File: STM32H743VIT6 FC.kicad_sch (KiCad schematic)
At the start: 88 parts, among them SW2 SW_Push, U1 TPS54302DDCR, U2 USBLC6-2SC6, U3 TPS54302DDCR, U3_MUX1 TPS2121RUXR

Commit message: mux no no no
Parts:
- removed D_5V1, D_5V_USB1: B340A-13-F, custom_Library:Schottky BA340 SMA_L4.4-W2.6-LS5.0-RD, symbol custom_Library:B340A-13-F
- removed MUX_C2: 100n, Capacitor_SMD:C_0603_1608Metric, symbol Device:C_Small
- removed MUX_R10: 60, Resistor_SMD:R_0603_1608Metric, symbol Device:R_Small
- removed MUX_R6: 13k, Resistor_SMD:R_0603_1608Metric, symbol Device:R_Small
- removed MUX_R7, MUX_R9: 5k, Resistor_SMD:R_0603_1608Metric, symbol Device:R_Small
- removed MUX_R8: 43k, Resistor_SMD:R_0603_1608Metric, symbol Device:R_Small
- removed U3_MUX1: TPS2121RUXR, TPS2121RUXR:RUX0012A, symbol ul_TPS2121RUXR:TPS2121RUXR
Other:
- note removed: "Diodes: 40V/3A 500mV 850mW"
- note removed: "Power Mux"
- note removed: "Power Path"

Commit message: nez
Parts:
- 5V_R8: value 13k3 -> 13k
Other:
- note added: "BAT -> 5.2V @3A"
- note removed: "BAT -> 5V @3A"
- moved on the sheet: 3V3_C4, 3v3_C3, 5V_C10, 5V_C11, 5V_C12, 5V_C7, 5V_C8, 5V_C9, 5V_L2, 5V_R5, 5V_R6, 5V_R7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

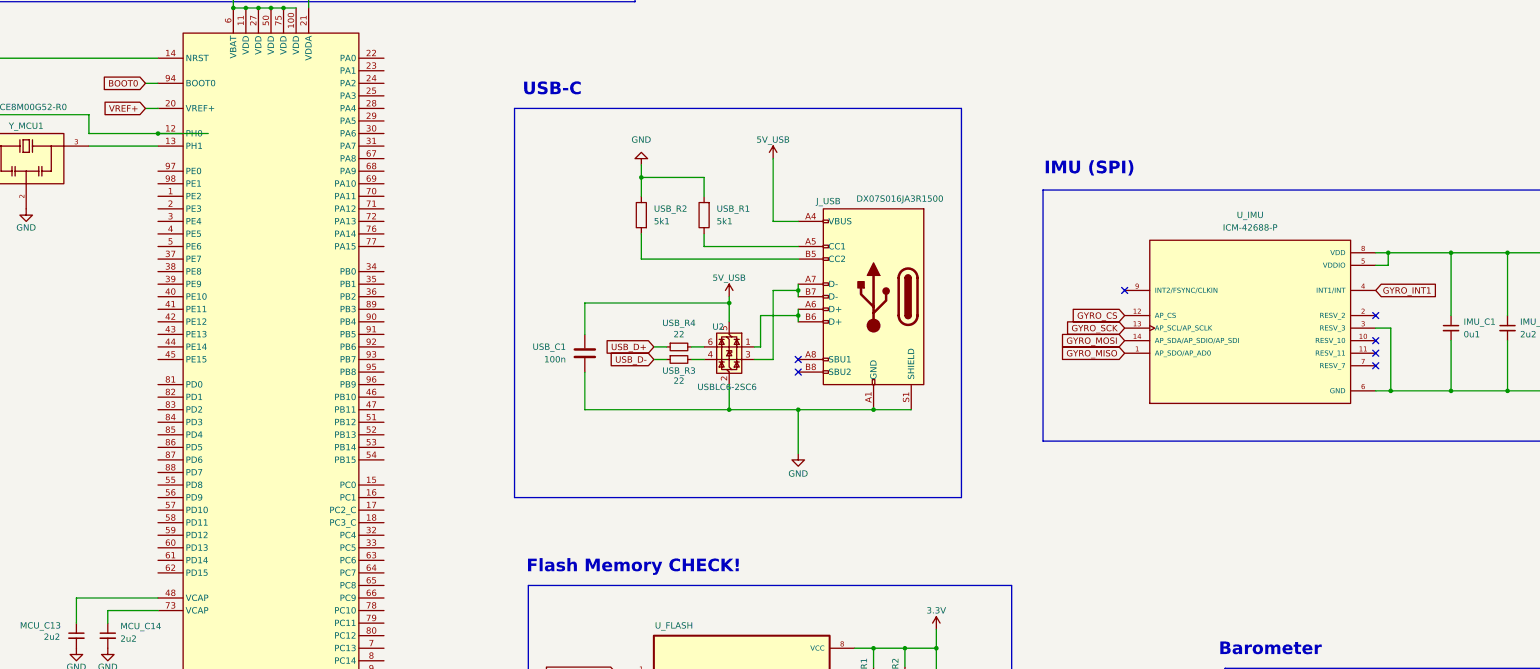
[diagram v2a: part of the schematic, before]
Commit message: Verified and connected IMU.
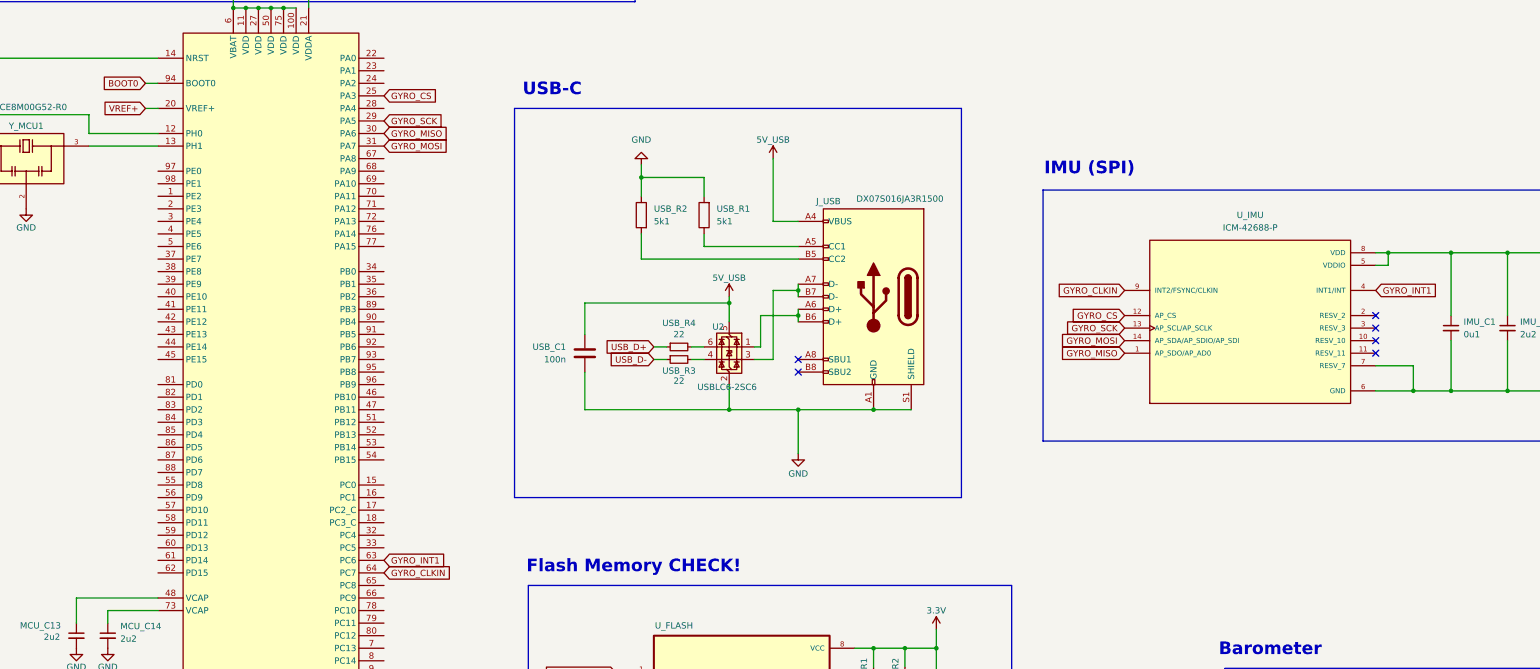
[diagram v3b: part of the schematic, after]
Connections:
- net GND: now also U_IMU.7 (RESV_7); no longer U_IMU.3 (RESV_3)
- net GYRO_CS: now also U_STM32.25 (PA3)
- net GYRO_INT1: now also U_STM32.63 (PC6)
- net GYRO_MISO: now also U_STM32.30 (PA6)
- net GYRO_MOSI: now also U_STM32.31 (PA7)
- net GYRO_SCK: now also U_STM32.29 (PA5)
- net GYRO_CLKIN: now reaches U_STM32.64 (PC7)
- net GYRO_CLKIN: now also U_IMU.9 (INT2/FSYNC/CLKIN)
- no-connect marks 9 -> 8
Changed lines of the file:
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@@
 	)
 	(junction
-		(at 102.87 93.98)
-		(diameter 0)
-		(color 0 0 0 0)
-	)
-	(junction
 		(at 487.68 323.85)
 		(diameter 0)
@@
 	)
 	(junction
-		(at 352.298 146.05)
-		(diameter 0)
-		(color 0 0 0 0)
-	)
-	(junction
 		(at 165.1 62.23)
 		(diameter 0)
@@
 	)
 	(junction
+		(at 356.87 146.05)
+		(diameter 0)
+		(color 0 0 0 0)
+	)
+	(junction
 		(at 88.9 54.61)
 		(diameter 0)
@@
 	)
 	(no_connect
+		(at 349.25 133.35)
+	)
+	(no_connect
 		(at 349.25 135.89)
 	)
@@
 	)
 	(no_connect
-		(at 298.45 125.73)
-	)
-	(no_connect
-		(at 349.25 140.97)
-	)
-	(no_connect
 		(at 347.98 334.01)
 	)
@@
 	(wire
 		(pts
-			(xy 349.25 133.35) (xy 352.298 133.35)
-		)
-		(stroke
-			(width 0)
-			(type default)
-		)
-	)
-	(wire
-		(pts
 			(xy 505.46 339.09) (xy 505.46 340.36)
 		)
@@
 	(wire
 		(pts
-			(xy 113.03 93.98) (xy 102.87 93.98)
-		)
-		(stroke
-			(width 0)
-			(type default)
-		)
-	)
-	(wire
-		(pts
 			(xy 260.35 198.12) (xy 260.35 205.74)
 		)
@@
 	(wire
 		(pts
+			(xy 356.87 146.05) (xy 364.49 146.05)
+		)
+		(stroke
+			(width 0)
+			(type default)
+		)
+	)
+	(wire
+		(pts
 			(xy 210.82 139.7) (xy 213.36 139.7)
 		)
@@
 	(wire
 		(pts
-			(xy 34.29 124.46) (xy 40.64 124.46)
+			(xy 88.9 93.98) (xy 102.87 93.98)
 		)
 		(stroke
@@
 	(wire
 		(pts
-			(xy 367.03 222.25) (xy 367.03 224.79)
+			(xy 34.29 124.46) (xy 40.64 124.46)
 		)
 		(stroke
@@
 	(wire
 		(pts
-			(xy 402.59 400.05) (xy 414.02 400.05)
+			(xy 367.03 222.25) (xy 367.03 224.79)
 		)
 		(stroke
@@
 	(wire
 		(pts
-			(xy 46.99 120.65) (xy 40.64 120.65)
+			(xy 402.59 400.05) (xy 414.02 400.05)
 		)
 		(stroke
@@
 	(wire
 		(pts
-			(xy 224.79 137.16) (xy 223.52 137.16)
+			(xy 46.99 120.65) (xy 40.64 120.65)
 		)
 		(stroke
@@
 	(wire
 		(pts
-			(xy 349.25 146.05) (xy 352.298 146.05)
+			(xy 224.79 137.16) (xy 223.52 137.16)
 		)
 		(stroke
@@
 	(wire
 		(pts
-			(xy 352.298 133.35) (xy 352.298 146.05)
-		)
-		(stroke
-			(width 0)
-			(type default)
-		)
-	)
-	(wire
-		(pts
 			(xy 364.49 224.79) (xy 367.03 224.79)
 		)
@@
 	(wire
 		(pts
+			(xy 349.25 140.97) (xy 356.87 140.97)
+		)
+		(stroke
+			(width 0)
+			(type default)
+		)
+	)
+	(wire
+		(pts
 			(xy 367.03 213.614) (xy 367.03 217.17)
 		)
@@
 	(wire
 		(pts
+			(xy 356.87 140.97) (xy 356.87 146.05)
+		)
+		(stroke
+			(width 0)
+			(type default)
+		)
+	)
+	(wire
+		(pts
 			(xy 31.75 260.35) (xy 31.75 262.89)
 		)
@@
 	(wire
 		(pts
-			(xy 352.298 146.05) (xy 364.49 146.05)
+			(xy 349.25 146.05) (xy 356.87 146.05)
 		)
 		(stroke
@@
 	(wire
 		(pts
-			(xy 102.87 93.98) (xy 88.9 93.98)
-		)
-		(stroke
-			(width 0)
-			(type default)
-		)
-	)
-	(wire
-		(pts
 			(xy 444.5 323.85) (xy 444.5 326.39)
 		)
@@
 		)
 	)
+	(global_label "GYRO_SCK"
+		(shape input)
+		(at 148.59 91.44 0)
+		(fields_autoplaced yes)
+		(effects
+			(font
+				(size 1.27 1.27)
+			)
+			(justify left)
+		)
+		(property "Intersheetrefs" "${INTERSHEET_REFS}"
+			(at 161.2514 91.44 0)
+			(effects
+				(font
+					(size 1.27 1.27)
+				)
+				(justify left)
+				(hide yes)
+			)
+		)
+	)
+	(global_label "GYRO_MISO"
+		(shape input)
+		(at 148.59 93.98 0)
+		(fields_autoplaced yes)
+		(effects
+			(font
+				(size 1.27 1.27)
+			)
+			(justify left)
+		)
+		(property "Intersheetrefs" "${INTERSHEET_REFS}"
+			(at 162.0981 93.98 0)
+			(effects
+				(font
+					(size 1.27 1.27)
+				)
+				(justify left)
+				(hide yes)
+			)
+		)
+	)
 	(global_label "VREF+"
 		(shape input)
@@
 		)
 	)
+	(global_label "GYRO_CS"
+		(shape input)
+		(at 148.59 86.36 0)
+		(fields_autoplaced yes)
+		(effects
+			(font
+				(size 1.27 1.27)
+			)
+			(justify left)
+		)
+		(property "Intersheetrefs" "${INTERSHEET_REFS}"
+			(at 159.9814 86.36 0)
+			(effects
+				(font
+					(size 1.27 1.27)
+				)
+				(justify left)
+				(hide yes)
+			)
+		)
+	)
 	(global_label "BOOT0"
 		(shape input)
@@
 		)
 	)
+	(global_label "GYRO_MOSI"
+		(shape input)
+		(at 148.59 96.52 0)
+		(fields_autoplaced yes)
+		(effects
+			(font
+				(size 1.27 1.27)
+			)
+			(justify left)
+		)
+		(property "Intersheetrefs" "${INTERSHEET_REFS}"
+			(at 162.0981 96.52 0)
+			(effects
+				(font
+					(size 1.27 1.27)
+				)
+				(justify left)
+				(hide yes)
+			)
+		)
+	)
 	(global_label "I2C1_SCL"
 		(shape input)
@@
 		)
 	)
+	(global_label "GYRO_INT1"
+		(shape input)
+		(at 148.59 180.34 0)
+		(fields_autoplaced yes)
+		(effects
+			(font
+				(size 1.27 1.27)
+			)
+			(justify left)
+		)
+		(property "Intersheetrefs" "${INTERSHEET_REFS}"
+			(at 161.6143 180.34 0)
+			(effects
+				(font
+					(size 1.27 1.27)
+				)
+				(justify left)
+				(hide yes)
+			)
+		)
+	)
 	(global_label "GYRO_MOSI"
 		(shape input)
@@
 		)
 	)
+	(global_label "GYRO_CLKIN"
+		(shape input)
+		(at 298.45 125.73 180)
+		(fields_autoplaced yes)
+		(effects
+			(font
+				(size 1.27 1.27)
+			)
+			(justify right)
+		)
+		(property "Intersheetrefs" "${INTERSHEET_REFS}"
+			(at 284.0347 125.73 0)
+			(effects
+				(font
+					(size 1.27 1.27)
+				)
+				(justify right)
+				(hide yes)
+			)
+		)
+	)
 	(global_label "I2C1_SDA"
 		(shape input)
@@
 				(hide yes)
 			)
+		)
+	)
+	(global_label "GYRO_CLKIN"
+		(shape input)
+		(at 148.59 182.88 0)
+		(fields_autoplaced yes)
+		(effects
+			(font
+				(size 1.27 1.27)
+			)
+			(justify left)
+		)
+		(property "Intersheetrefs" "${INTERSHEET_REFS}"
+			(at 163.0053 182.88 0)
+			(effects
+				(font
+					(size 1.27 1.27)
+				)
+				(justify left)
+				(hide yes)
+			)

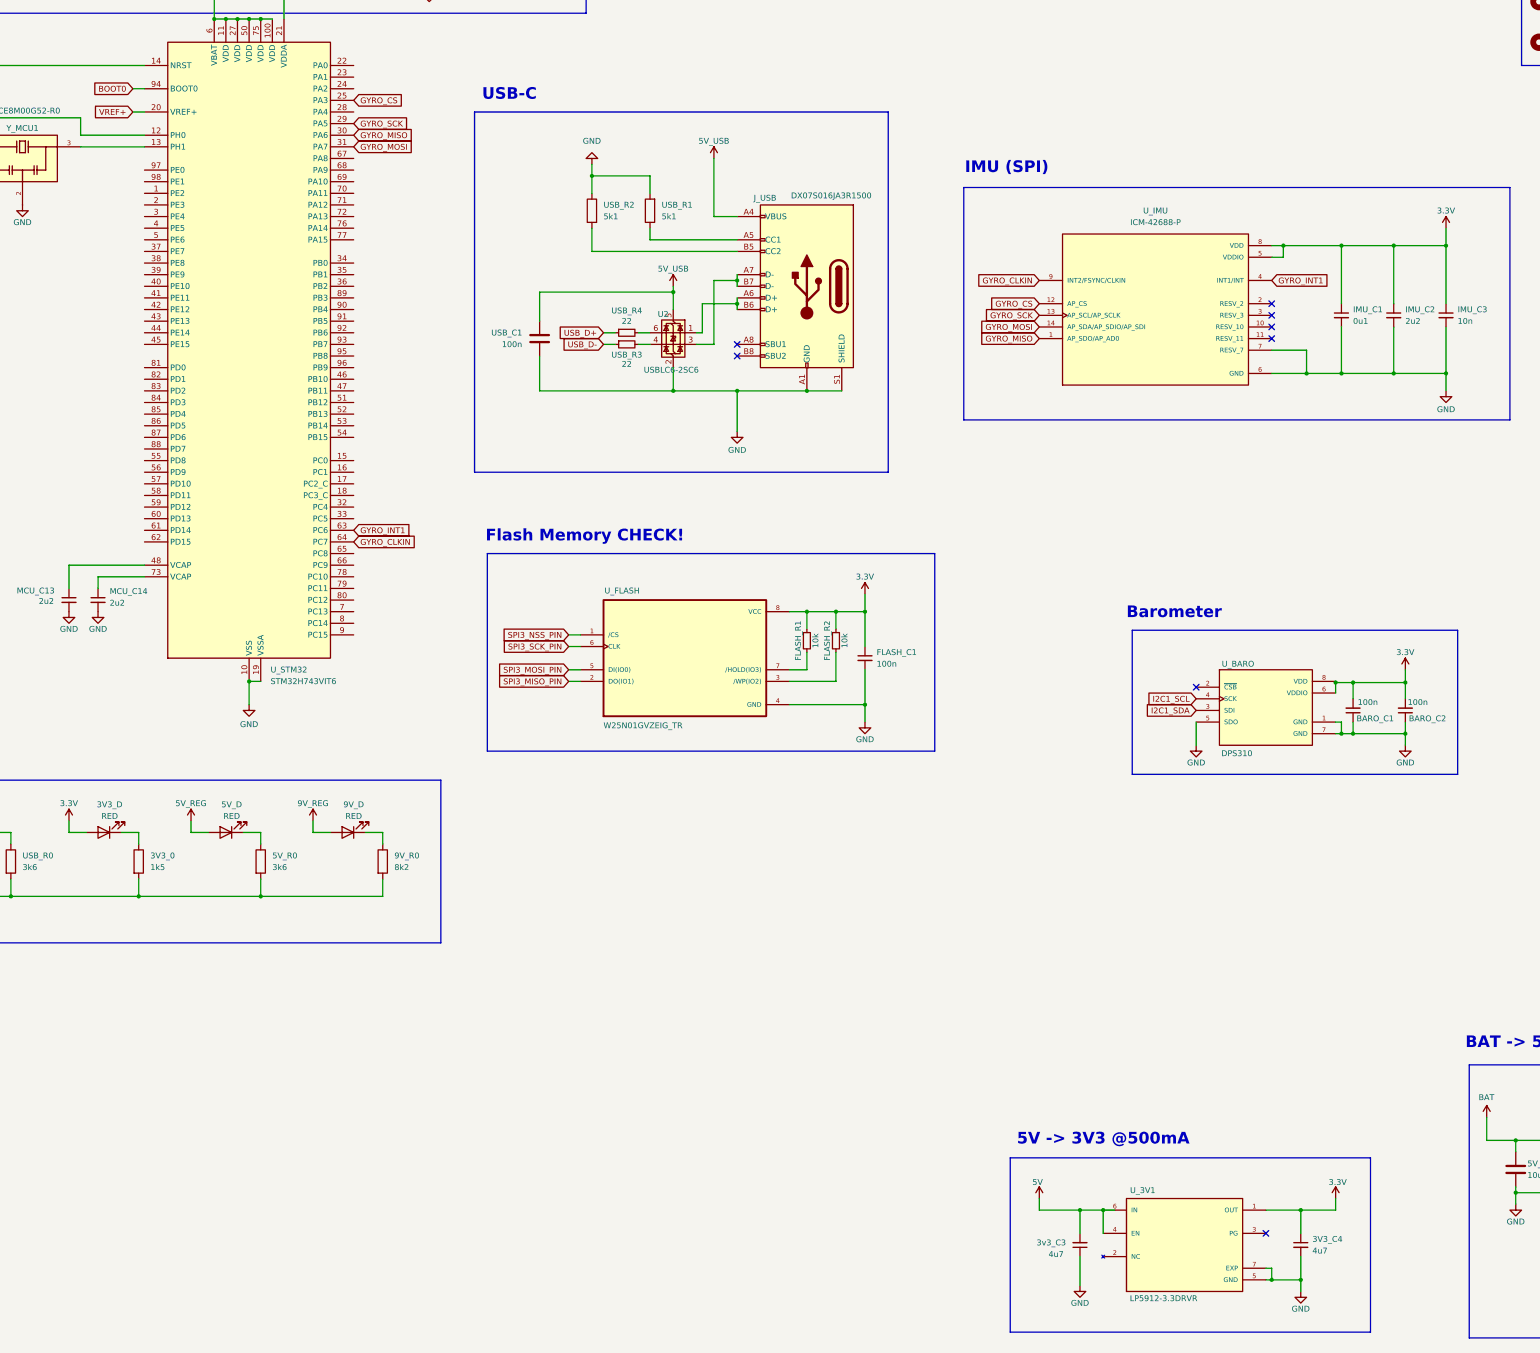
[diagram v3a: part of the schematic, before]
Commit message: Verified baro, flash, and power. Added minimal pinout of the MCU.
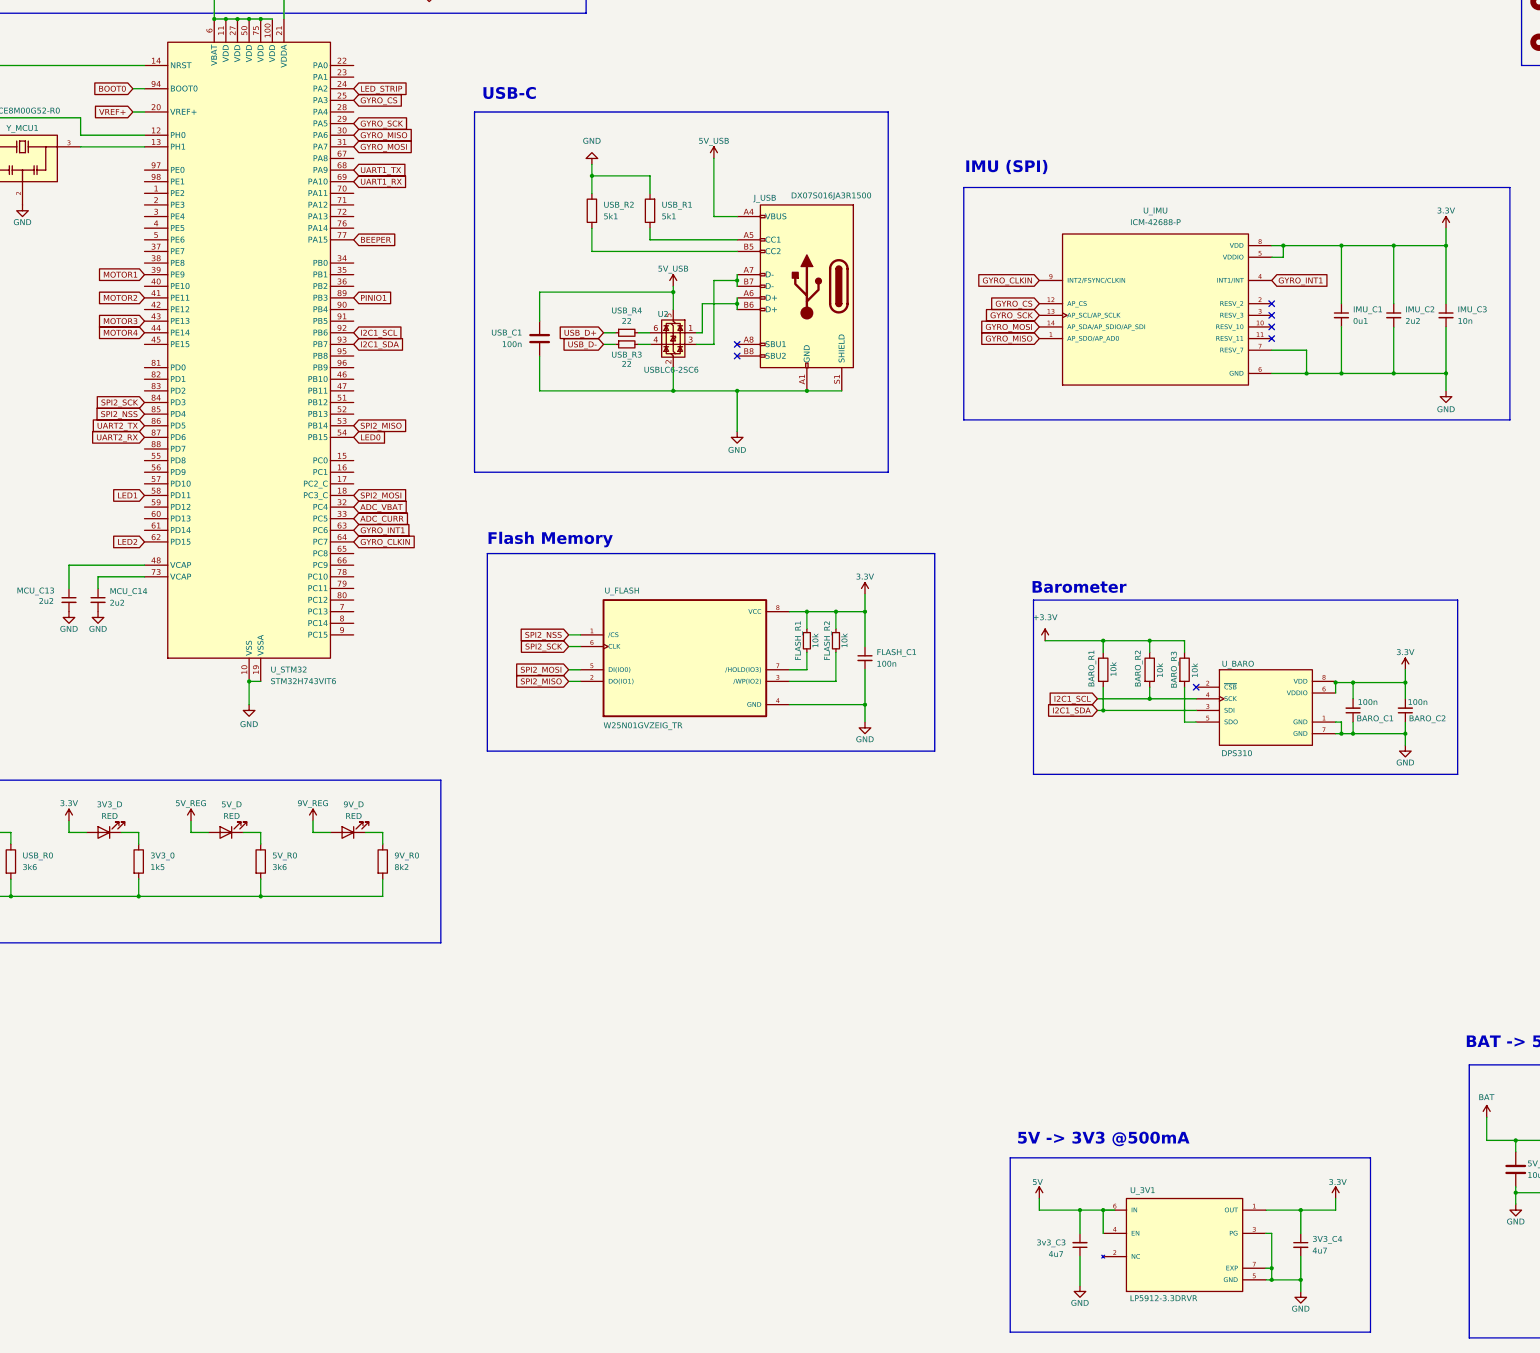
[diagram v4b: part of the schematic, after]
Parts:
- added BARO_R1, BARO_R2, BARO_R3: 10k, Resistor_SMD:R_0603_1608Metric, symbol Device:R
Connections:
- net SPI3_MISO_PIN is gone; now on net SPI2_MISO: U_FLASH.2 (DO(IO1))
- net SPI3_MOSI_PIN is gone; now on net SPI2_MOSI: U_FLASH.5 (DI(IO0))
- net SPI3_NSS_PIN is gone; now on net SPI2_NSS: U_FLASH.1 (/CS)
- net SPI3_SCK_PIN is gone; now on net SPI2_SCK: U_FLASH.6 (CLK)
- net GND: now also U_3V1.3 (PG); no longer U_BARO.5 (SDO)
- net I2C1_SCL: now also U_STM32.92 (PB6), BARO_R2.2
- net I2C1_SDA: now also U_STM32.93 (PB7), BARO_R1.2
- net SPI2_MOSI: now reaches U_STM32.18 (PC3_C)
- net LED_STRIP: now reaches U_STM32.24 (PA2)
- net ADC_VBAT: now reaches U_STM32.32 (PC4)
- net ADC_CURR: now reaches U_STM32.33 (PC5)
- net MOTOR1: now reaches U_STM32.39 (PE9)
- net MOTOR2: now reaches U_STM32.41 (PE11)
- net MOTOR3: now reaches U_STM32.43 (PE13)
- net MOTOR4: now reaches U_STM32.44 (PE14)
- net SPI2_MISO: now reaches U_STM32.53 (PB14)
- net LED0: now reaches U_STM32.54 (PB15)
- net LED1: now reaches U_STM32.58 (PD11)
- net LED2: now reaches U_STM32.62 (PD15)
- net UART1_TX: now reaches U_STM32.68 (PA9)
- net UART1_RX: now reaches U_STM32.69 (PA10)
- net BEEPER: now reaches U_STM32.77 (PA15)
- net SPI2_SCK: now reaches U_STM32.84 (PD3)
- net SPI2_NSS: now reaches U_STM32.85 (PD4)
- net UART2_TX: now reaches U_STM32.86 (PD5)
- net UART2_RX: now reaches U_STM32.87 (PD6)
- net PINIO1: now reaches U_STM32.89 (PB3)
- new net: BARO_R3.2, U_BARO.5 (SDO)
- new net +3.3V: BARO_R1.1, BARO_R2.1, BARO_R3.1
- no-connect marks 8 -> 7
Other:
- note added: "Flash Memory"
- note removed: "Flash Memory CHECK!"

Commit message: 3.3V ldo
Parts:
- removed U_3V1: LP5912-3.3DRVR, custom_Library:LP59123.3_SON65P200X200X80-7N, symbol custom_Library:LP5912-3.3DRVR
- added U_3V1: LP5912-3.3DRV, Package_SON:WSON-6-1EP_2x2mm_P0.65mm_EP1x1.6mm_ThermalVias, symbol Regulator_Linear:LP5912-3.3DRV
- 3v3_C3: value 4u7 -> 1u
- 5V_C8, 5V_C9, 9V_C8, 9V_C9, IMU_C1: value 0u1 -> 100n
- renumbered 3V3_D to 3V3_D1, 5V_D to 5V_D1, 9V_D to 9V_D1, J_USB to J_USB1, MCU_D to MCU_D1, USB_D to USB_D1, U_BARO to U_BARO1, U_FLASH to U_FLASH1, U_IMU to U_IMU1
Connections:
- net 3.3V: now also U_3V1.1 (OUT)
- net 5V: now also U_3V1.4 (EN), U_3V1.6 (IN)
- net GND: now also U_3V1.5 (GND), U_3V1.7 (EP)
- no-connect marks 7 -> 8
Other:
- moved on the sheet: 3V3_C4, 3v3_C3, 5V_C10, 5V_C11, 5V_C12, 5V_C7, 5V_C8, 5V_C9, 5V_L2, 5V_R5, 5V_R6, 5V_R7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
